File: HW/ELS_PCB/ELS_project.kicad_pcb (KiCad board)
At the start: 4 copper layers, 95.6 x 86.1 mm, 66 parts, among them CN1 MX205V-5.0-03P-GN01-CU-A, CN2 MX250-3.5-08P-B-GY01-CU-A, CN3 MX250-3.5-06P-B-GY01-CU-A, CN4 MX205V-5.0-03P-GN01-CU-A, J1 Conn_01x05_Pin, J2 Conn_01x03_Pin, J3 Conn_01x04_Pin, Q1 2N7002, Q2 2N7002, Q3 2N7002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

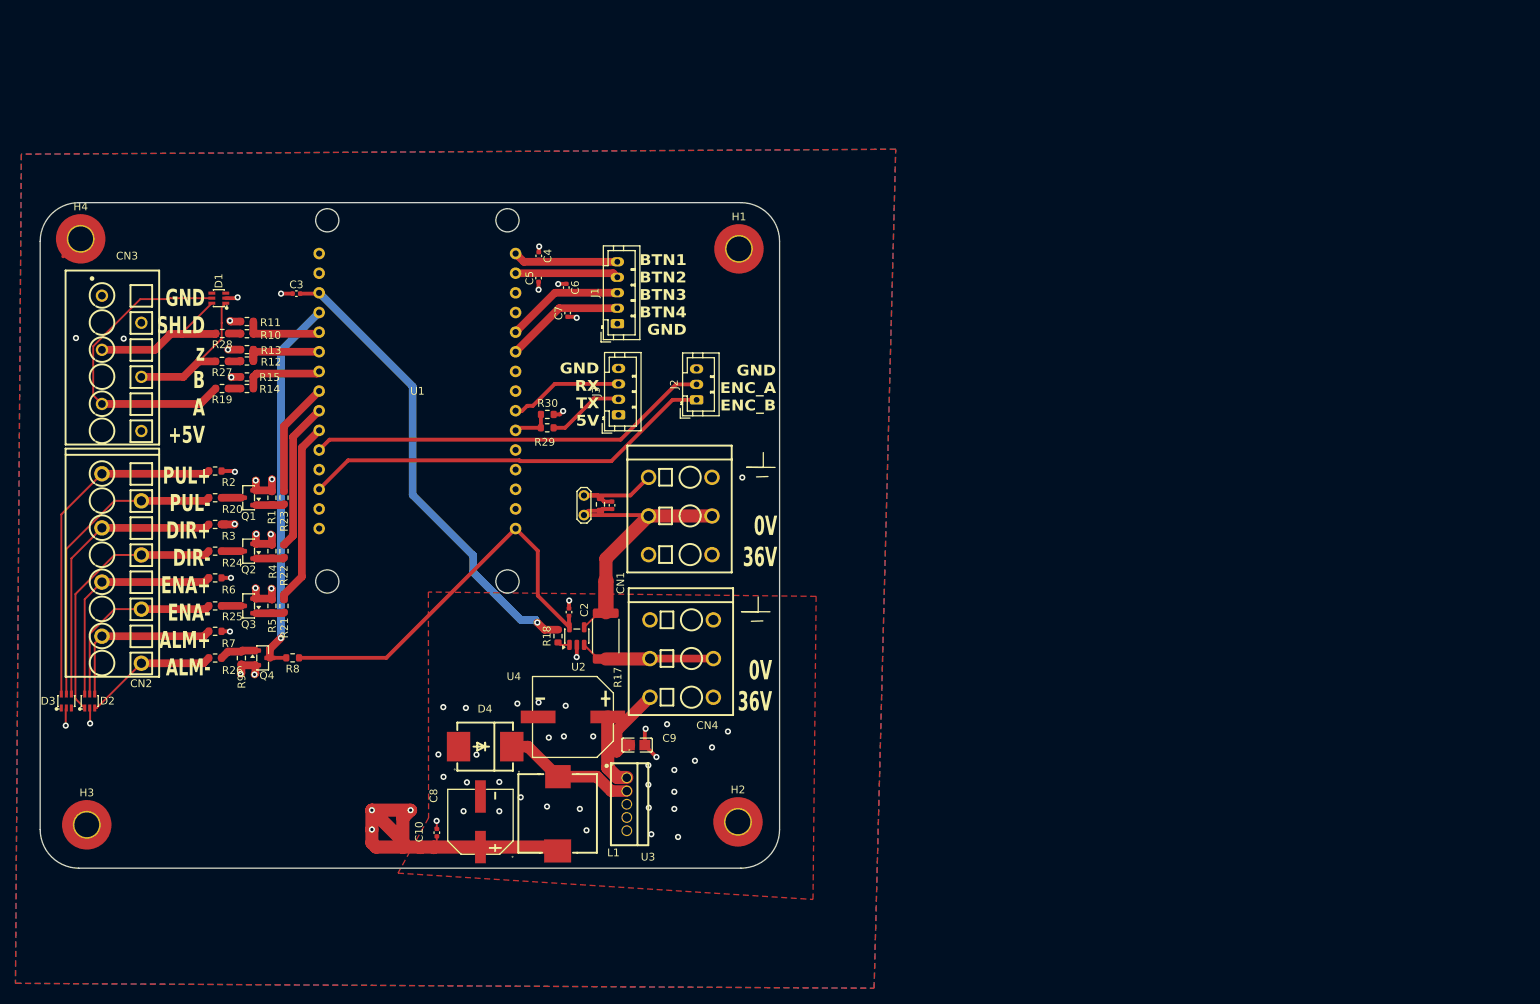
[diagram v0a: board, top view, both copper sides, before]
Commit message: redesigned the powerstage sinse the org got realy hot. using newer parts
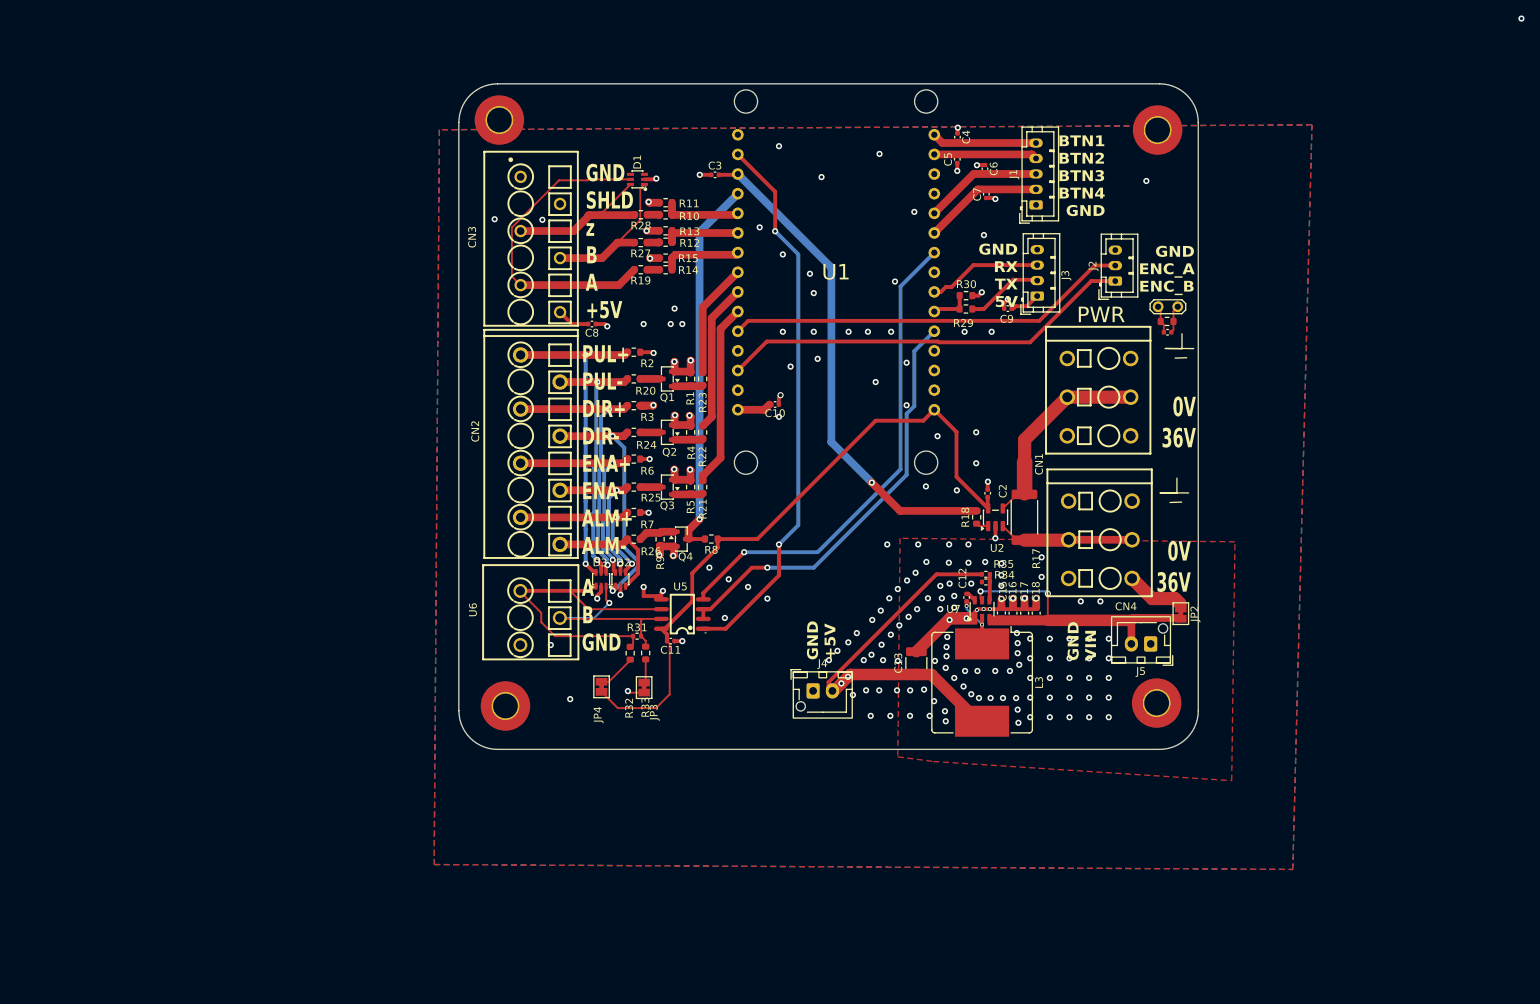
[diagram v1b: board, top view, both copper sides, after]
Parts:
- removed D4: SS510, LCSC:SMC_L7.1-W6.2-LS8.1-R-RD
- removed L1: SLO1040H680MTT, LCSC:IND-SMD_L10.8-W10.0
- removed U3: LM2596HVT-5.0, LCSC:TO-220-5L_L10.2-W4.5-P1.71-L
- removed U4: EFVH100ADA101M10C0, LCSC:CAP-SMD_BD10.0-L10.3-W10.3-FD
- added C11: 1uF, Capacitor_SMD:C_0402_1005Metric, F.Cu at (123.6, 123.1)
- added C12: GRM155R71C104KA88D, Capacitor_SMD:C_0402_1005Metric, F.Cu at (161.9, 117.5)
- added C13: GRM32ER61C476KE15L, Capacitor_SMD:C_1210_3225Metric, F.Cu at (155.4, 126.0)
- added C15: MSASU168SB5105MTNA01, Capacitor_SMD:C_0603_1608Metric, F.Cu at (166.4, 119.5)
- added C16: MSASU168SB5105MTNA01, Capacitor_SMD:C_0603_1608Metric, F.Cu at (167.9, 119.5)
- added C17: MSASU168SB5105MTNA01, Capacitor_SMD:C_0603_1608Metric, F.Cu at (169.4, 119.5)
- added C18: GRM188R72A104KA35D, Capacitor_SMD:C_0603_1608Metric, F.Cu at (170.9, 119.5)
- added J4: Conn_01x02_Pin, Connector_JST:JST_XH_B2B-XH-AM_1x02_P2.50mm_Vertical, F.Cu at (142.1, 129.6)
- added J5: Conn_01x02_Pin, Connector_JST:JST_XH_B2B-XH-AM_1x02_P2.50mm_Vertical, F.Cu at (185.7, 123.5)
- added JP2: SolderJumper_2_Bridged, Jumper:SolderJumper-2_P1.3mm_Bridged_Pad1.0x1.5mm, F.Cu at (189.6, 119.6)
- added JP3: SolderJumper_2_Bridged, Jumper:SolderJumper-2_P1.3mm_Bridged_Pad1.0x1.5mm, F.Cu at (120.2, 129.2)
- added JP4: SolderJumper_2_Bridged, Jumper:SolderJumper-2_P1.3mm_Bridged_Pad1.0x1.5mm, F.Cu at (114.7, 129.1)
- added L3: SRR1208-120ML, Inductor_SMD:L_Bourns_SRR1208_12.7x12.7mm, F.Cu at (163.9, 128.5)
- added R31: 100Ω, Resistor_SMD:R_0402_1005Metric, F.Cu at (119.3, 122.5)
- added R32: 1kΩ, Resistor_SMD:R_0603_1608Metric, F.Cu at (118.4, 124.7)
- added R33: 1kΩ, Resistor_SMD:R_0603_1608Metric, F.Cu at (120.4, 124.7)
- added R34: 22.1 kΩ, Resistor_SMD:R_0402_1005Metric, F.Cu at (164.4, 115.5)
- added R35: 174 kΩ, Resistor_SMD:R_0402_1005Metric, F.Cu at (164.4, 114.5)
- added U5: SP3485EN-L/TR, LCSC:SOIC-8_L5.0-W4.0-P1.27-LS6.0-BL, F.Cu at (125.1, 119.6)
- added U6: MX250-3.5-03P-B-GY01-CU-A, LCSC:CONN-TH_3P-P3.50_MX250-3.5-03P-B-GY01-CU-A, F.Cu at (106.8, 120.1)
- added U7: LMR51420XDDCR, LCSC:SOT-23-6_L2.9-W1.6-P0.95-LS2.8-BL, F.Cu at (163.9, 119.0)
- C10: value 100nF -> 1uF
- C8: value EEHZK1V181P -> 1uF; footprint LCSC:CAP-SMD_BD8.0-L8.3-W8.3-FD -> Capacitor_SMD:C_0402_1005Metric
- C9: value 0805B391K101NT -> 1uF; footprint LCSC:C0805 -> Capacitor_SMD:C_0402_1005Metric
- R8: value 100k -> 10k
- moved JP1 80.6 mm to (189.2, 79.9), turned to 180 degrees
- moved R16 77.0 mm to (187.8, 81.8), turned to 180 degrees
- moved C1 75.2 mm to (187.9, 83.2), turned to 180 degrees
- moved C9 74.1 mm to (167.2, 80.1)
- moved D3 70.9 mm to (114.6, 115.1)
- moved C10 70.6 mm to (137.1, 92.5), turned to 180 degrees
- moved D2 70.4 mm to (117.1, 115.1)
- moved C8 66.0 mm to (113.5, 82.1), turned to 180 degrees
- moved C3 56.3 mm to (129.4, 62.8)
- moved CN1 56.3 mm to (179.0, 91.6)
- moved H2 56.3 mm to (186.5, 131.1)
- moved R17 56.3 mm to (169.4, 107.1)
- moved R29 56.3 mm to (161.8, 80.2)
- moved U2 56.3 mm to (165.6, 107.1)
- moved H3 56.3 mm to (102.3, 131.5)
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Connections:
- C8 pad 1: +5V -> GND
- C8 pad 2: GND -> +5V
- C9 pad 1: +36V -> GND
- C9 pad 2: GND -> +5V
- D3 pad 1: unconnected-(D3-Pad1) -> /485_A
- D3 pad 3: unconnected-(D3-Pad3) -> /485_B
- U1 pad 2: unconnected-(U1-GPIO36_ADC-CH0_SENS-VP_RTC-GPIO0-Pad2) -> /485_RX
- U1 pad 20: unconnected-(U1-GPIO4_ADC2-CH0_RTC-GPIO10-Pad20) -> /485_DE~{RE}
- U1 pad 24: unconnected-(U1-GPIO18_VSPI-CLK-Pad24) -> /485_TX
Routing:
- net Earth_Protective: track 314.9 -> 486.1 mm, vias 4 -> 3
- net /485_RX: track 0.00 -> 71.4 mm, vias 0 -> 2
- net /485_TX: track 0.00 -> 62.8 mm, vias 0 -> 1
- net /485_DE~{RE}: track 0.00 -> 54.8 mm, vias 0 -> 1
- net /485_A: track 0.00 -> 49.3 mm
- net /VIN: track 0.00 -> 40.4 mm, vias 0 -> 2
- net +3.3V: track 52.1 -> 86.3 mm
- net +36V: track 74.9 -> 45.7 mm
- net /485_B: track 0.00 -> 26.6 mm, vias 0 -> 1
- net GND: track 71.3 -> 91.0 mm, vias 55 -> 179
- net Net-(D4-K): track 17.3 -> 0.00 mm
- net +5V: track 53.5 -> 68.8 mm, vias 7 -> 6
- net /SW: track 0.00 -> 7.20 mm, vias 0 -> 2
- net /STEP_PUL-: track 39.9 -> 34.1 mm, vias 0 -> 2
- net Net-(JP4-A): track 0.00 -> 4.95 mm
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- added copper zone on In2.Cu, net GND
- removed copper zone on In2.Cu, net +36V
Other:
- board text added: "A B GND"
- board text added: "GND +5V"
- board text added: "GND VIN"
- board text added: "PWR"
